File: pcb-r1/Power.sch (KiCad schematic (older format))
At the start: 22 parts, among them P301 USB-MICRO-B, P302 ALT PWR, U301 FT232RQ, U302 MCP1700T-3302E

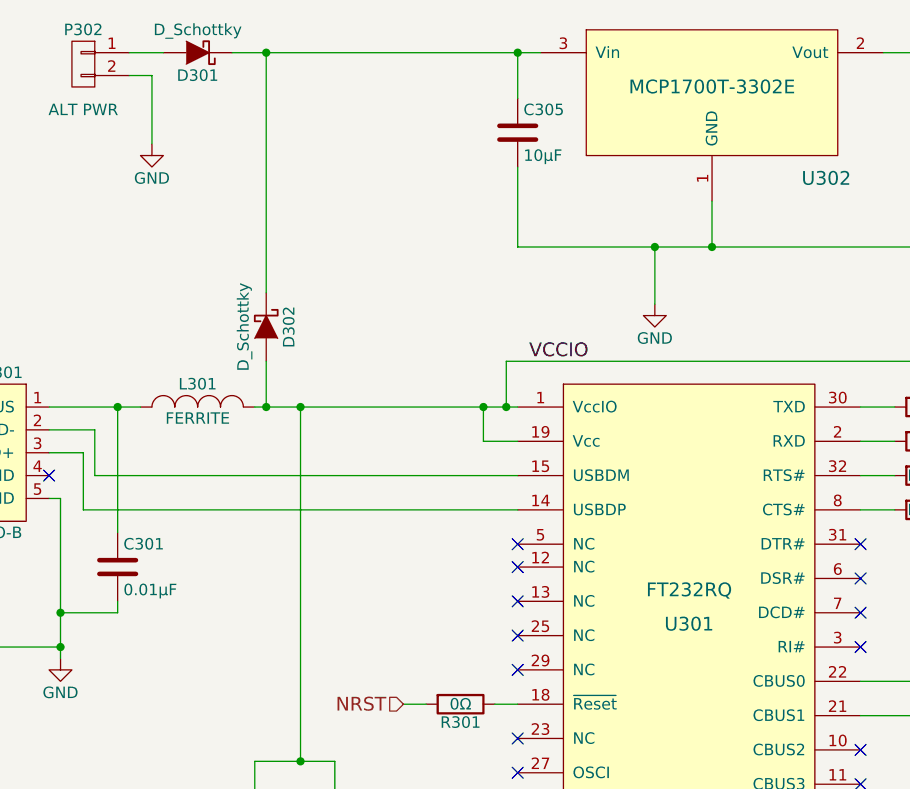
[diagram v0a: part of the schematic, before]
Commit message: Updated the parts for the BOM
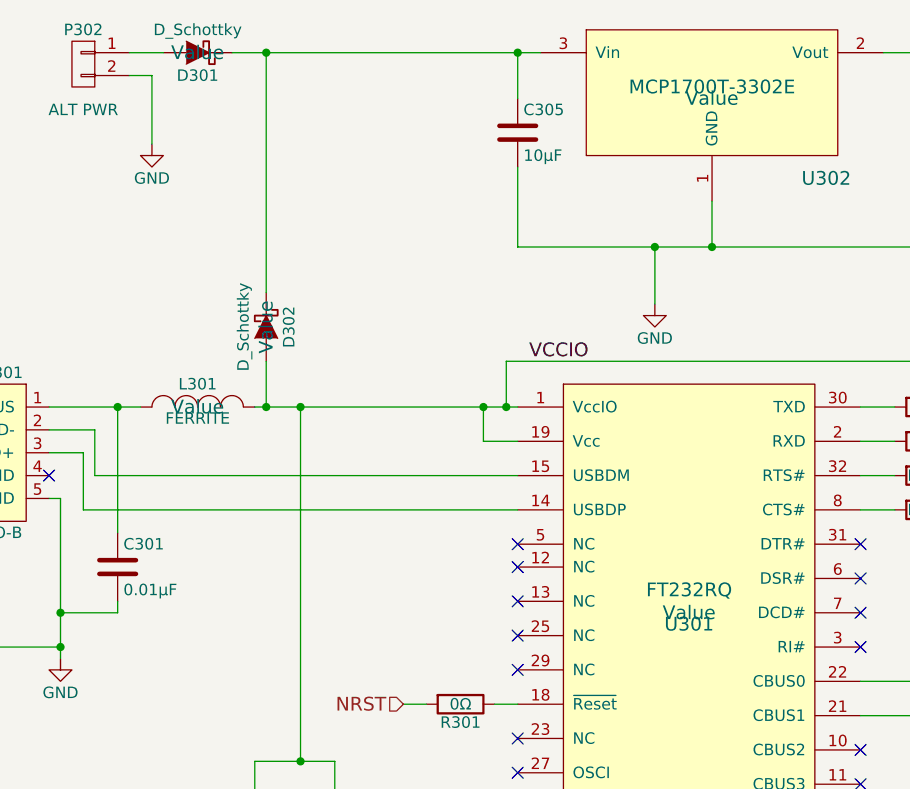
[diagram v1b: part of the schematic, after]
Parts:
- D301, D302: ConradPN (none) -> Value; DigiKeyPN (none) -> B130-FDICT-ND; Label (none) -> Value; MPN (none) -> B130-13-F
- L301: ConradPN (none) -> Value; DigiKeyPN (none) -> 732-4661-1-ND; Label (none) -> Value; MPN (none) -> 742792605
- U301: ConradPN (none) -> Value; DigiKeyPN (none) -> 768-1008-1-ND; Label (none) -> Value; MPN (none) -> FT232RQ-REEL
- U302: ConradPN (none) -> Value; DigiKeyPN (none) -> MCP1700T3302ETTCT-ND; Label (none) -> Value; MPN (none) -> MCP1700T-3302E/TT
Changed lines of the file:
@@
 F 2 "TO_SOT_Packages_SMD:SOT-23" H 5950 3300 60  0001 C CNN
 F 3 "" H 5950 3300 60  0000 C CNN
-F 4 "http://parts.io/detail/1370896/MCP1700T-3302E%2FTT" H 6050 3150 60  0001 C CNN "link"
+F 4 "MCP1700T-3302E/TT" H 6050 3150 60  0001 C CNN "MPN"
+F 5 "Value" H 6050 3150 60  0001 C CNN "ConradPN"
+F 6 "Value" H 6050 3150 60  0000 C CNN "Label"
+F 7 "http://parts.io/detail/1370896/MCP1700T-3302E%2FTT" H 6050 3150 60  0001 C CNN "link"
+F 8 "MCP1700T3302ETTCT-ND" H 6050 3150 60  0001 C CNN "DigiKeyPN"
 	1    6050 3150
 	1    0    0    -1
@@
 F 2 "Housings_DFN_QFN:QFN-32-1EP_5x5mm_Pitch0.5mm" H 5650 6000 60  0001 C CNN
 F 3 "http://www.ftdichip.com/Support/Documents/DataSheets/ICs/DS_FT232R.pdf" H 5650 6000 60  0001 C CNN
+F 4 "FT232RQ-REEL" H 5950 5400 60  0001 C CNN "MPN"
+F 5 "Value" H 5950 5400 60  0001 C CNN "ConradPN"
+F 6 "Value" H 5950 5400 60  0000 C CNN "Label"
+F 7 "768-1008-1-ND" H 5950 5400 60  0001 C CNN "DigiKeyPN"
 	1    5950 5400
 	1    0    0    -1
@@
 F 2 "Inductors_NEOSID:Neosid_Inductor_SM1206" H 3800 4500 60  0001 C CNN
 F 3 "" H 3800 4500 60  0000 C CNN
+F 4 "742792605" H 3800 4500 60  0001 C CNN "MPN"
+F 5 "Value" H 3800 4500 60  0001 C CNN "ConradPN"
+F 6 "Value" H 3800 4500 60  0000 C CNN "Label"
+F 7 "732-4661-1-ND" H 3800 4500 60  0001 C CNN "DigiKeyPN"
 	1    3800 4500
 	1    0    0    -1
@@
 F 2 "Diodes_SMD:SMA_Standard" H 3800 2950 60  0001 C CNN
 F 3 "" H 3800 2950 60  0000 C CNN
+F 4 "B130-13-F" H 3800 2950 60  0001 C CNN "MPN"
+F 5 "Value" H 3800 2950 60  0001 C CNN "ConradPN"
+F 6 "Value" H 3800 2950 60  0000 C CNN "Label"
+F 7 "B130-FDICT-ND" H 3800 2950 60  0001 C CNN "DigiKeyPN"
 	1    3800 2950
 	-1   0    0    1
@@
 F 2 "Diodes_SMD:SMA_Standard" H 4100 4150 60  0001 C CNN
 F 3 "" H 4100 4150 60  0000 C CNN
+F 4 "B130-13-F" H 4100 4150 60  0001 C CNN "MPN"
+F 5 "Value" H 4100 4150 60  0001 C CNN "ConradPN"
+F 6 "Value" H 4100 4150 60  0000 C CNN "Label"
+F 7 "B130-FDICT-ND" H 4100 4150 60  0001 C CNN "DigiKeyPN"
 	1    4100 4150
 	0    1    1    0

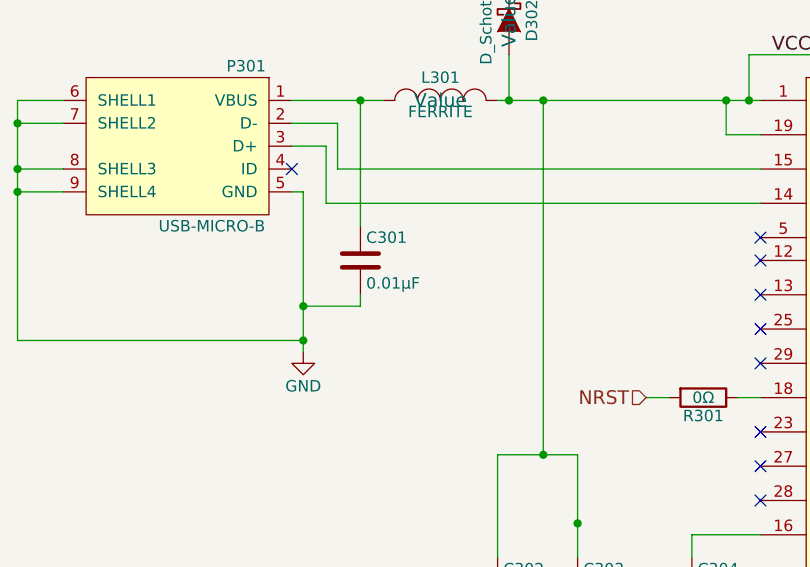
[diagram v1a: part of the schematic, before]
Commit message: Updated the parts with further DigiKeyPN
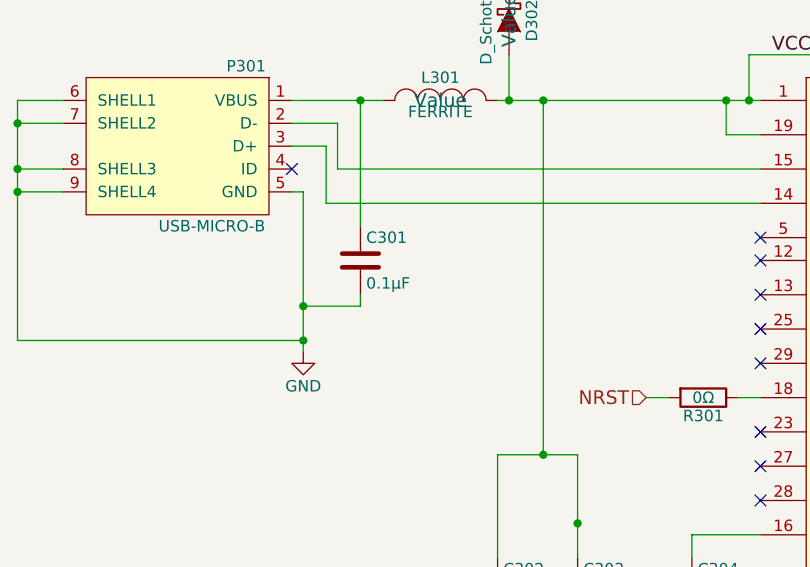
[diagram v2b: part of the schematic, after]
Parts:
- C301: value 0.01μF -> 0.1μF
- C302, C304: DigiKeyPN (none) -> 478-1395-1-ND
- C303: DigiKeyPN (none) -> 1276-1856-1-ND
- C305: DigiKeyPN (none) -> 1276-2865-1-ND
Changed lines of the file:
@@
 F 2 "Capacitors_SMD:C_1210" H 5238 3150 30  0001 C CNN
 F 3 "" H 5200 3300 60  0000 C CNN
+F 4 "1276-2865-1-ND" H 5200 3300 60  0001 C CNN "DigiKeyPN"
 	1    5200 3300
 	1    0    0    -1
@@
 P 3450 5200
 F 0 "C301" H 3475 5300 50  0000 L CNN
-F 1 "0.01μF" H 3475 5100 50  0000 L CNN
+F 1 "0.1μF" H 3475 5100 50  0000 L CNN
 F 2 "Capacitors_SMD:C_0805" H 3488 5050 30  0001 C CNN
 F 3 "" H 3450 5200 60  0000 C CNN
@@
 F 2 "Capacitors_SMD:C_0805" H 4088 6500 30  0001 C CNN
 F 3 "" H 4050 6650 60  0000 C CNN
+F 4 "478-1395-1-ND" H 4050 6650 60  0001 C CNN "DigiKeyPN"
 	1    4050 6650
 	1    0    0    -1
@@
 F 2 "Capacitors_SMD:C_0805" H 4438 6500 30  0001 C CNN
 F 3 "" H 4400 6650 60  0000 C CNN
+F 4 "1276-1856-1-ND" H 4400 6650 60  0001 C CNN "DigiKeyPN"
 	1    4400 6650
 	1    0    0    -1
@@
 F 2 "Capacitors_SMD:C_0805" H 4938 6500 30  0001 C CNN
 F 3 "" H 4900 6650 60  0000 C CNN
+F 4 "478-1395-1-ND" H 4900 6650 60  0001 C CNN "DigiKeyPN"
 	1    4900 6650
 	1    0    0    -1

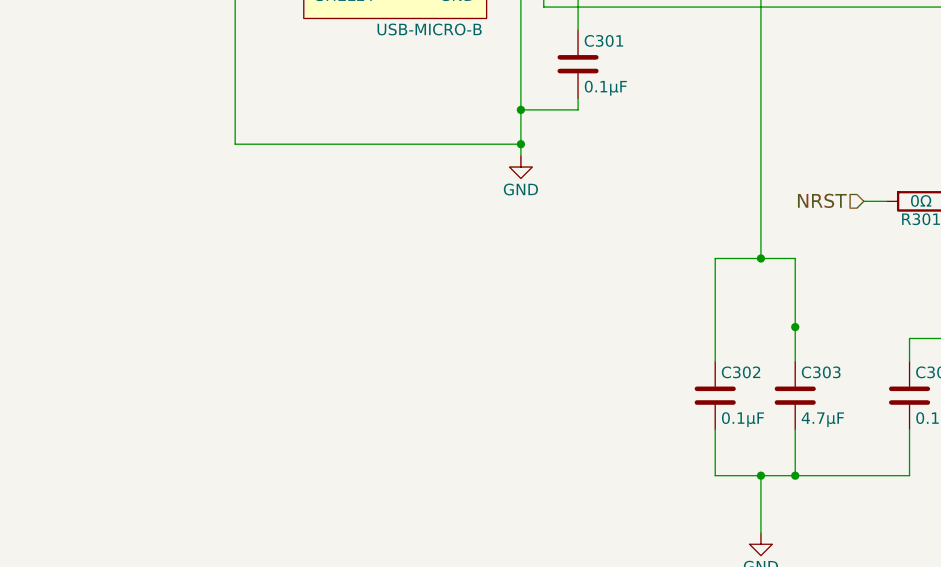
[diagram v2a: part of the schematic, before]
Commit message: Made the correction to the Tx Rx on the schematic and added a comment regarding the Ferrite Bead
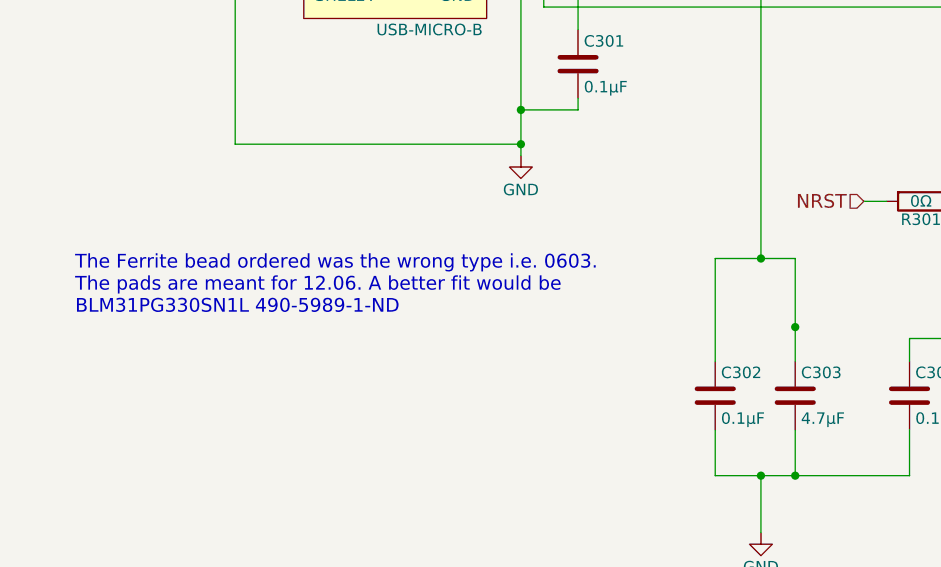
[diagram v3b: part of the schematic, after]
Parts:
- L301: Link (none) -> Value; Voltage (none) -> Value
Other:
- note added: "The Ferrite bead ordered was the wrong type i.e. 0603. \nThe pads are meant for 12.06. A better fit would be \nBLM31PG330SN1L 490-5989-1-ND"
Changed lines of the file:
@@
 F 2 "Inductors_NEOSID:Neosid_Inductor_SM1206" H 3800 4500 60  0001 C CNN
 F 3 "" H 3800 4500 60  0000 C CNN
-F 4 "742792605" H 3800 4500 60  0001 C CNN "MPN"
-F 5 "Value" H 3800 4500 60  0001 C CNN "ConradPN"
-F 6 "Value" H 3800 4500 60  0000 C CNN "Label"
-F 7 "732-4661-1-ND" H 3800 4500 60  0001 C CNN "DigiKeyPN"
+F 4 "732-4661-1-ND" H 3800 4500 60  0001 C CNN "DigiKeyPN"
+F 5 "Value" H 3800 4500 60  0001 C CNN "Voltage"
+F 6 "Value" H 3800 4500 60  0001 C CNN "ConradPN"
+F 7 "Value" H 3800 4500 60  0001 C CNN "Link"
+F 8 "742792605" H 3800 4500 60  0001 C CNN "MPN"
+F 9 "Value" H 3800 4500 60  0000 C CNN "Label"
 	1    3800 4500
 	1    0    0    -1
@@
 NoConn ~ 5200 6250
 NoConn ~ 5200 6100
+Text Notes 1250 6300 0    60   ~ 0
+The Ferrite bead ordered was the wrong type i.e. 0603. \nThe pads are meant for 12.06. A better fit would be \nBLM31PG330SN1L 490-5989-1-ND
 $EndSCHEMATC
